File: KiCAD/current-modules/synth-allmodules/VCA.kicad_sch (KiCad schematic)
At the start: 0 parts

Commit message: VCA components
Additions:
- Added appropriate components for VCA module
Changes:
- None
Removals:
- None
NOTES:
- Components still need to be arranged and circuit connected!
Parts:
- added C26: C, symbol Device:C
- added C27: C_Polarized, symbol Device:C_Polarized
- added D30: 1N914, Diode_THT:D_DO-35_SOD27_P7.62mm_Horizontal, symbol Diode:1N914
- added Q9: 2N3906, Package_TO_SOT_THT:TO-92_Inline, symbol Transistor_BJT:2N3906
- added R52: R, symbol Device:R
- added RV24: R_Potentiometer, symbol Device:R_Potentiometer
- added SW5: SW_SPST, symbol Switch:SW_SPST
- added U10: TL071, symbol Amplifier_Operational:TL071
- added U9: TL072, symbol Amplifier_Operational:TL072

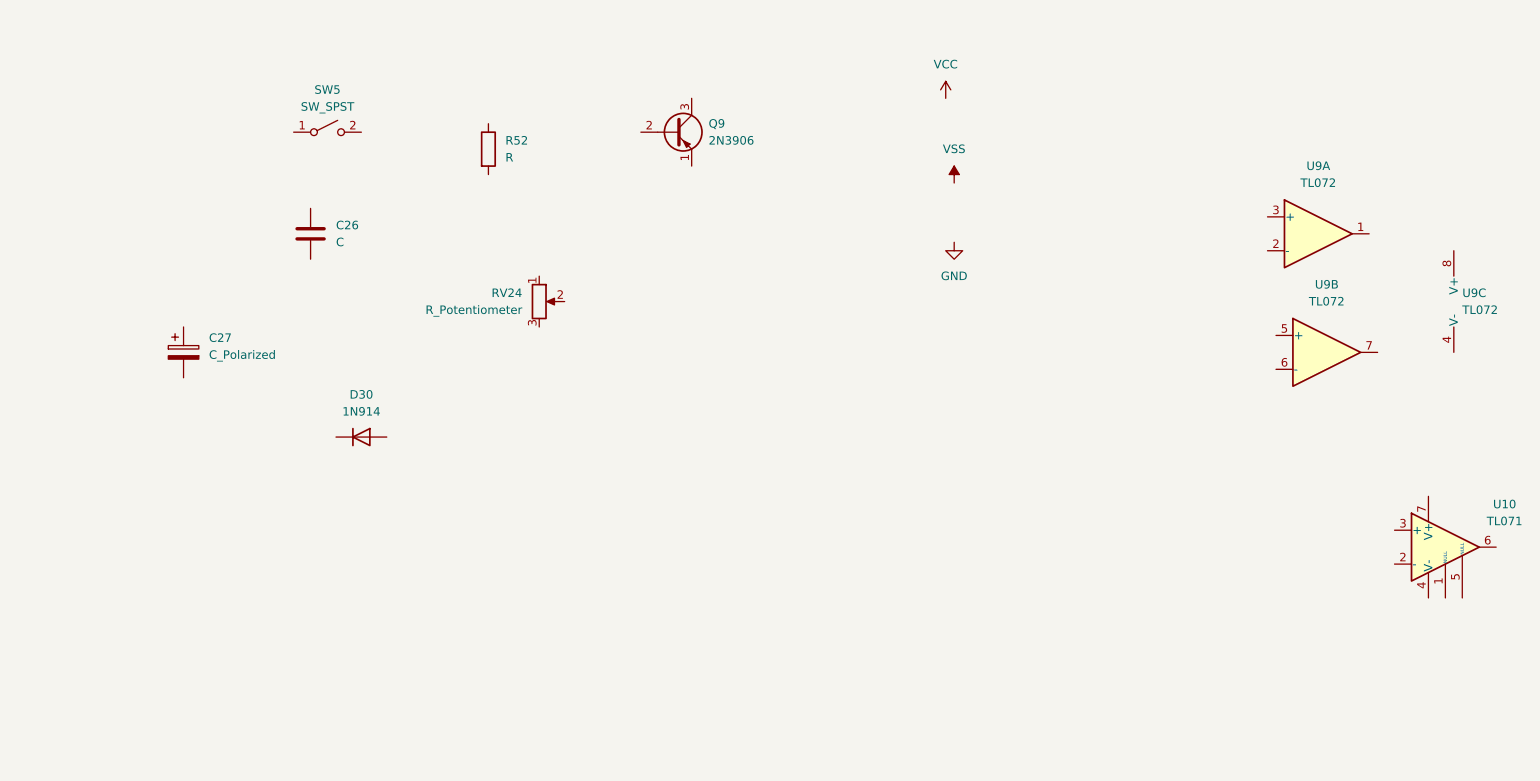
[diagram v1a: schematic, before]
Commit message: VCA wired minus jacks
Additions:
- Connected up the VCA circuit
Changes:
- None
Removals:
- None
NOTES:
- Audio jacks are still missing!
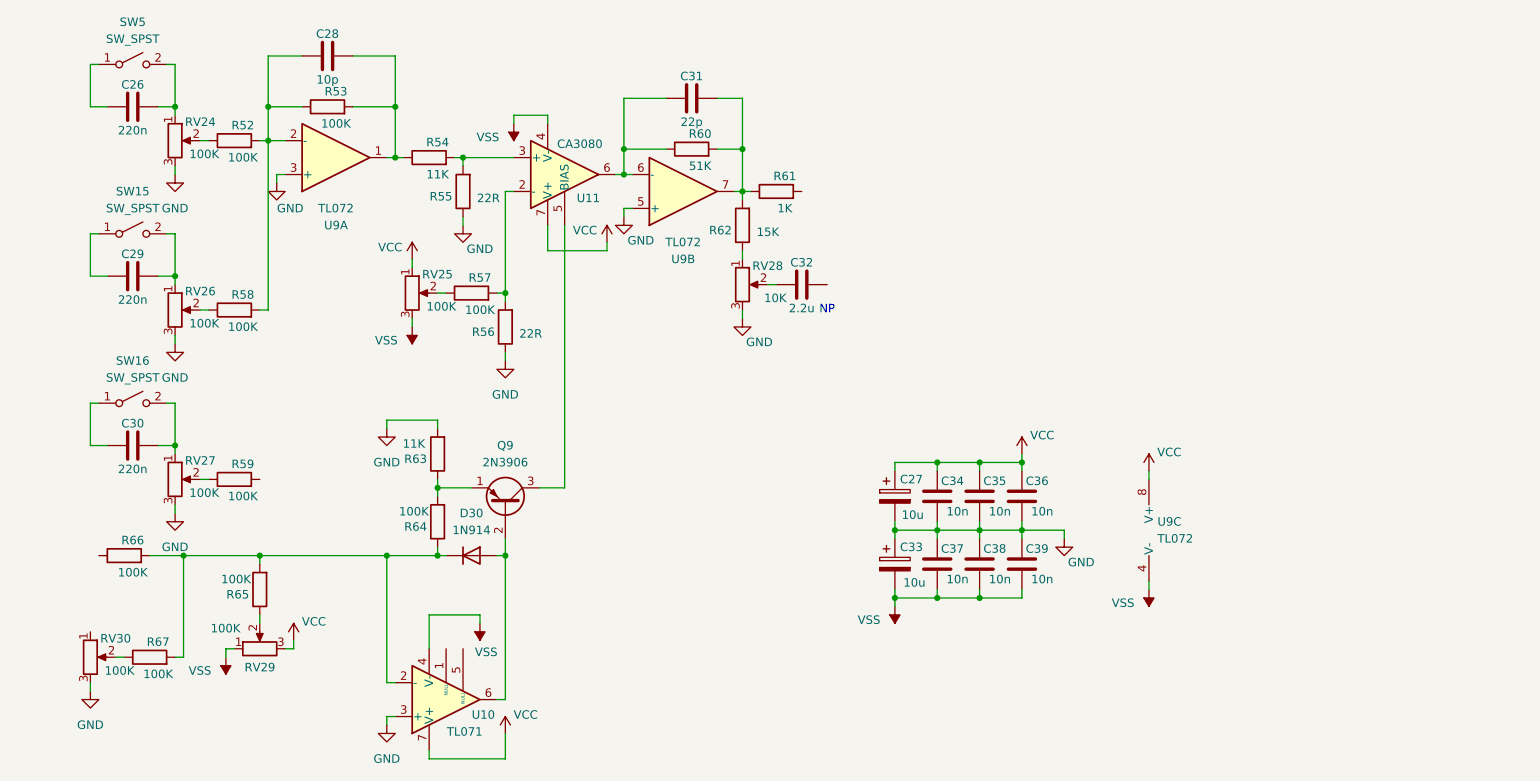
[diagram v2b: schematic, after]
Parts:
- added C28: 10p, symbol Device:C
- added C29, C30: 220n, symbol Device:C
- added C31: 22p, symbol Device:C
- added C32: 2.2u, symbol Device:C
- added C33: 10u, symbol Device:C_Polarized
- added C34, C35, C36, C37, C38, C39: 10n, symbol Device:C
- added R53, R57, R58, R59, R64, R65, R66, R67: 100K, symbol Device:R
- added R54, R63: 11K, symbol Device:R
- added R55, R56: 22R, symbol Device:R
- added R60: 51K, symbol Device:R
- added R61: 1K, symbol Device:R
- added R62: 15K, symbol Device:R
- added RV25, RV26, RV27, RV29, RV30: 100K, symbol Device:R_Potentiometer
- added RV28: 10K, symbol Device:R_Potentiometer
- added SW15, SW16: SW_SPST, symbol Switch:SW_SPST
- added U11: CA3080, symbol Amplifier_Operational:CA3080
- C26: value C -> 220n
- C27: value C_Polarized -> 10u
- R52: value R -> 100K
- RV24: value R_Potentiometer -> 100K
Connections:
- net GND: now also C27.2, RV24.3, U10.3 (+), U9.3 (+), U9.5 (+), C33.1, C34.1, C35.1, C36.1, C37.2, C38.2, C39.2, R55.1, R56.1, R63.2, RV26.3, RV27.3, RV28.3, RV30.3
- net VCC: now also C27.1, U10.7 (V+), U9.8 (V+), C34.2, C35.2, C36.2, RV25.1, RV29.3, U11.7 (V+)
- net VSS: now also U10.4 (V-), U9.4 (V-), C33.2, C37.1, C38.1, C39.1, RV25.3, RV29.1, U11.4 (V-)
- net at U9.6 (-): now also C31.1, R60.1, U11.6
- net at U9.7: now also C31.2, R60.2, R61.1, R62.2
- net at D30.1 (K): now also U10.2 (-), R64.1, R65.2, R66.2, R67.2
- net at D30.2 (A): now also Q9.2 (B), U10.6
- net at C26.1: now also SW5.1 (A)
- net at C26.2: now also RV24.1, SW5.2 (B)
- net at Q9.1 (E): now also R63.1, R64.2
- net at Q9.3 (C): now also U11.5 (BIAS)
- net at R52.1: now also RV24.2
- net at R52.2: now also U9.2 (-), C28.1, R53.1, R58.2
- net at U9.1: now also C28.2, R53.2, R54.1
- new net: R56.2, R57.2, U11.2 (-)
- new net: R67.1, RV30.2
- new net: R59.1, RV27.2
- new net: C29.2, RV26.1, SW15.2 (B)
- new net: R58.1, RV26.2
- new net: C29.1, SW15.1 (A)
- new net: R54.2, R55.2, U11.3 (+)
- new net: R57.1, RV25.2
- new net: R62.1, RV28.1
- new net: C32.1, RV28.2
- new net: R65.1, RV29.2
- new net: C30.2, RV27.1, SW16.2 (B)
- new net: C30.1, SW16.1 (A)
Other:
- note added: "NP"
- moved on the sheet: C26, C27, D30, Q9, R52, RV24, SW5, U10, U9A, U9B, U9C

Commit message: VCA IOs labelled
Additions:
- IO and potentiometer labels for VCA module
Changes:
- None
Removals:
- None
NOTES:
- Audio jacks are still missing!
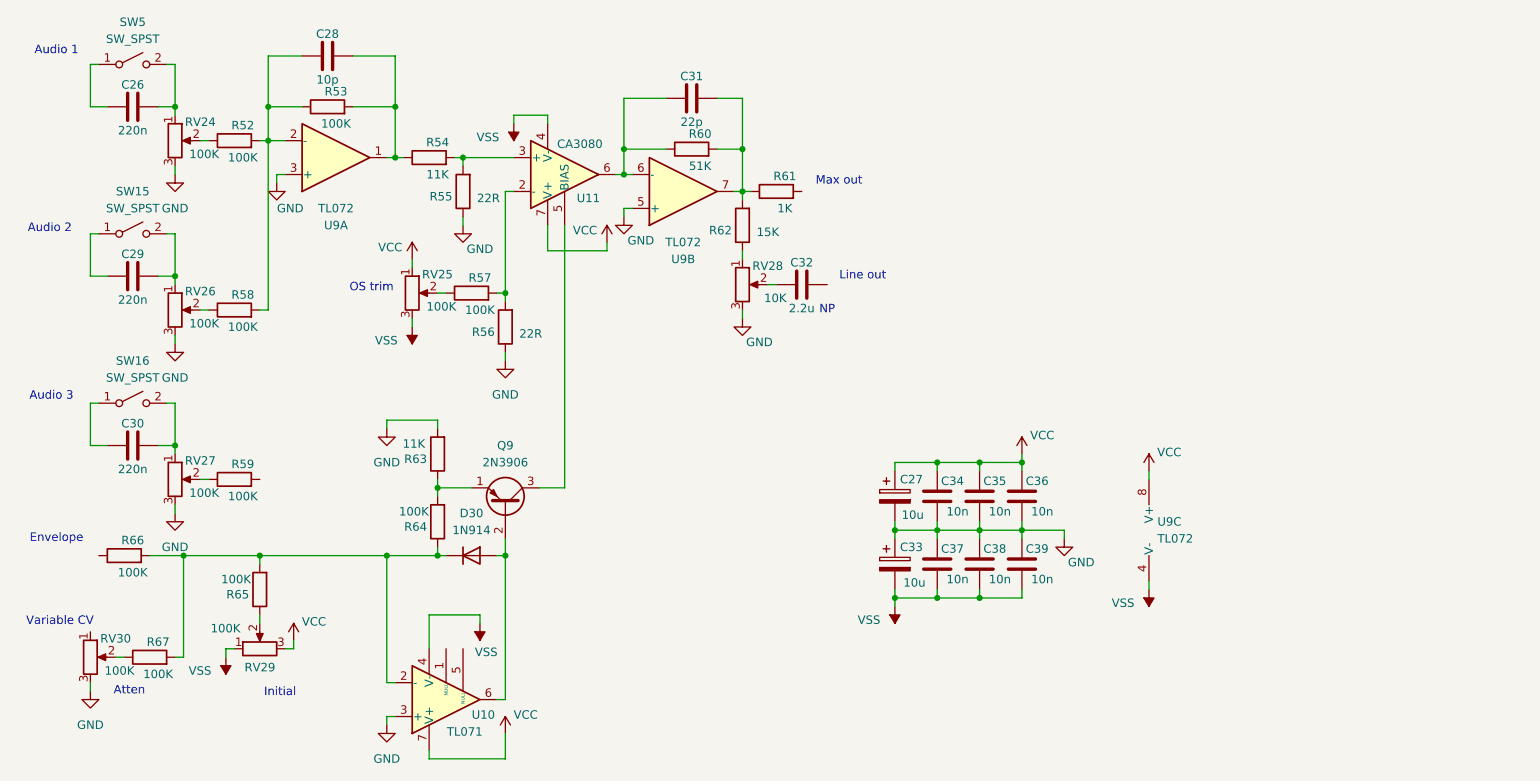
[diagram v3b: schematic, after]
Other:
- note added: "Atten"
- note added: "Audio 1"
- note added: "Audio 2"
- note added: "Audio 3"
- note added: "Envelope"
- note added: "Initial"
- note added: "Line out"
- note added: "Max out"
- note added: "OS trim"
- note added: "Variable CV"
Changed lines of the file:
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@@
+		)
+	)
+	(text "OS trim"
+		(exclude_from_sim no)
+		(at 67.564 58.928 0)
+		(effects
+			(font
+				(size 1.27 1.27)
+			)
+		)
+	)
+	(text "Initial"
+		(exclude_from_sim no)
+		(at 53.848 119.634 0)
+		(effects
+			(font
+				(size 1.27 1.27)
+			)
+		)
+	)
+	(text "Audio 2"
+		(exclude_from_sim no)
+		(at 19.304 50.038 0)
+		(effects
+			(font
+				(size 1.27 1.27)
+			)
+		)
+	)
+	(text "Audio 3"
+		(exclude_from_sim no)
+		(at 19.558 75.184 0)
+		(effects
+			(font
+				(size 1.27 1.27)
+			)
+		)
+	)
+	(text "Max out"
+		(exclude_from_sim no)
+		(at 137.668 42.926 0)
+		(effects
+			(font
+				(size 1.27 1.27)
+			)
+		)
+	)
+	(text "Audio 1"
+		(exclude_from_sim no)
+		(at 20.32 23.368 0)
+		(effects
+			(font
+				(size 1.27 1.27)
+			)
+		)
+	)
+	(text "Atten"
+		(exclude_from_sim no)
+		(at 31.242 119.38 0)
+		(effects
+			(font
+				(size 1.27 1.27)
+			)
+		)
+	)
+	(text "Envelope"
+		(exclude_from_sim no)
+		(at 20.32 96.52 0)
+		(effects
+			(font
+				(size 1.27 1.27)
+			)
+		)
+	)
+	(text "Variable CV"
+		(exclude_from_sim no)
+		(at 20.828 108.966 0)
+		(effects
+			(font
+				(size 1.27 1.27)
+			)
+		)
+	)
+	(text "Line out"
+		(exclude_from_sim no)
+		(at 141.224 57.15 0)
+		(effects
+			(font
+				(size 1.27 1.27)
+			)
 		)
 	)
